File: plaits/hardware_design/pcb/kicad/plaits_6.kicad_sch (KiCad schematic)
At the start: 22 parts

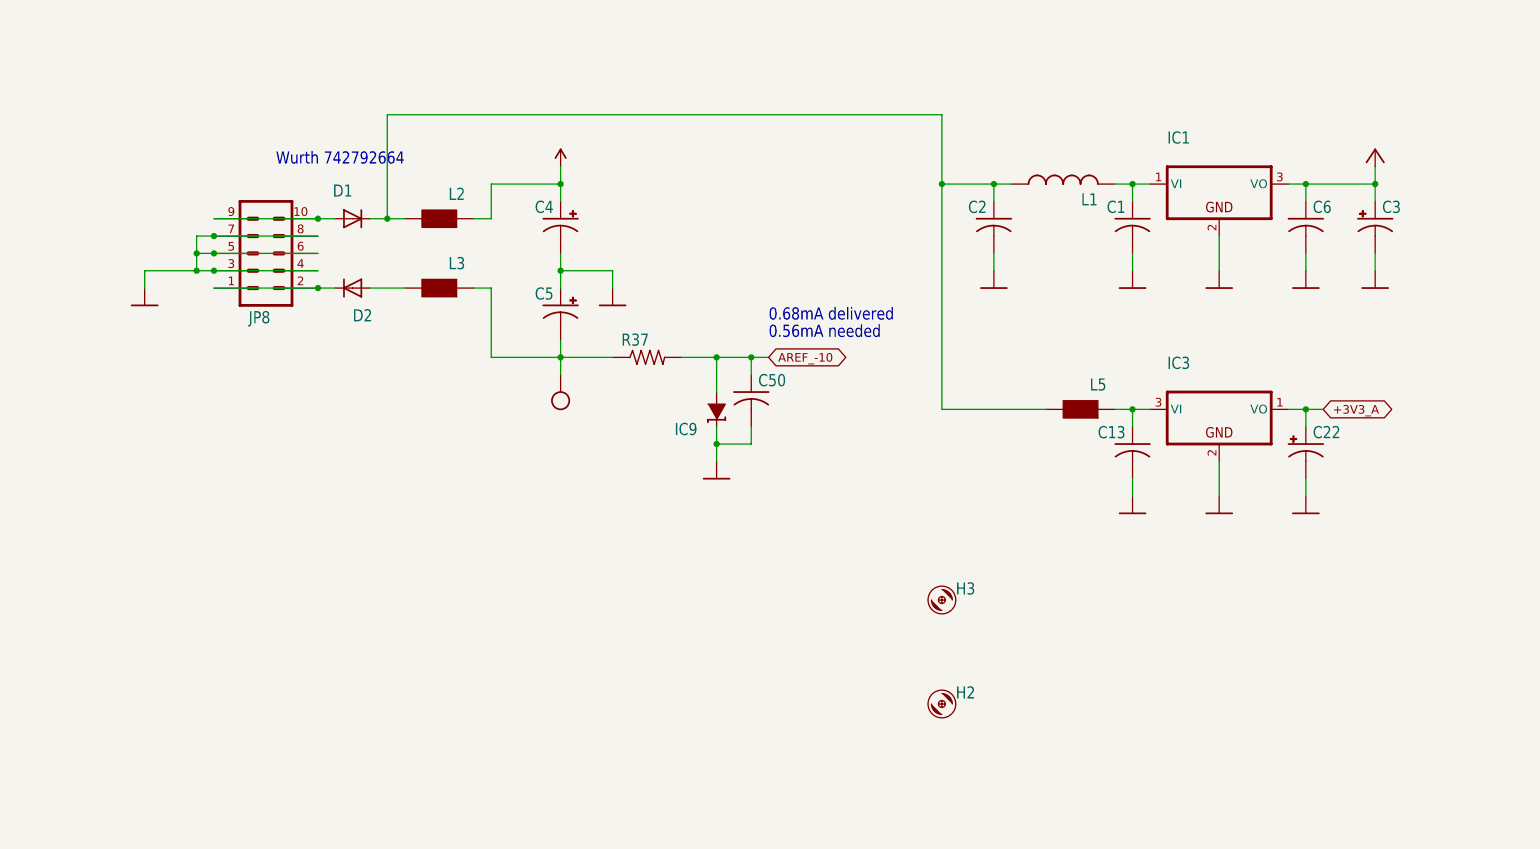
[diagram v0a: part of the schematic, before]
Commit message: plaits resized panasonic A -> B caps
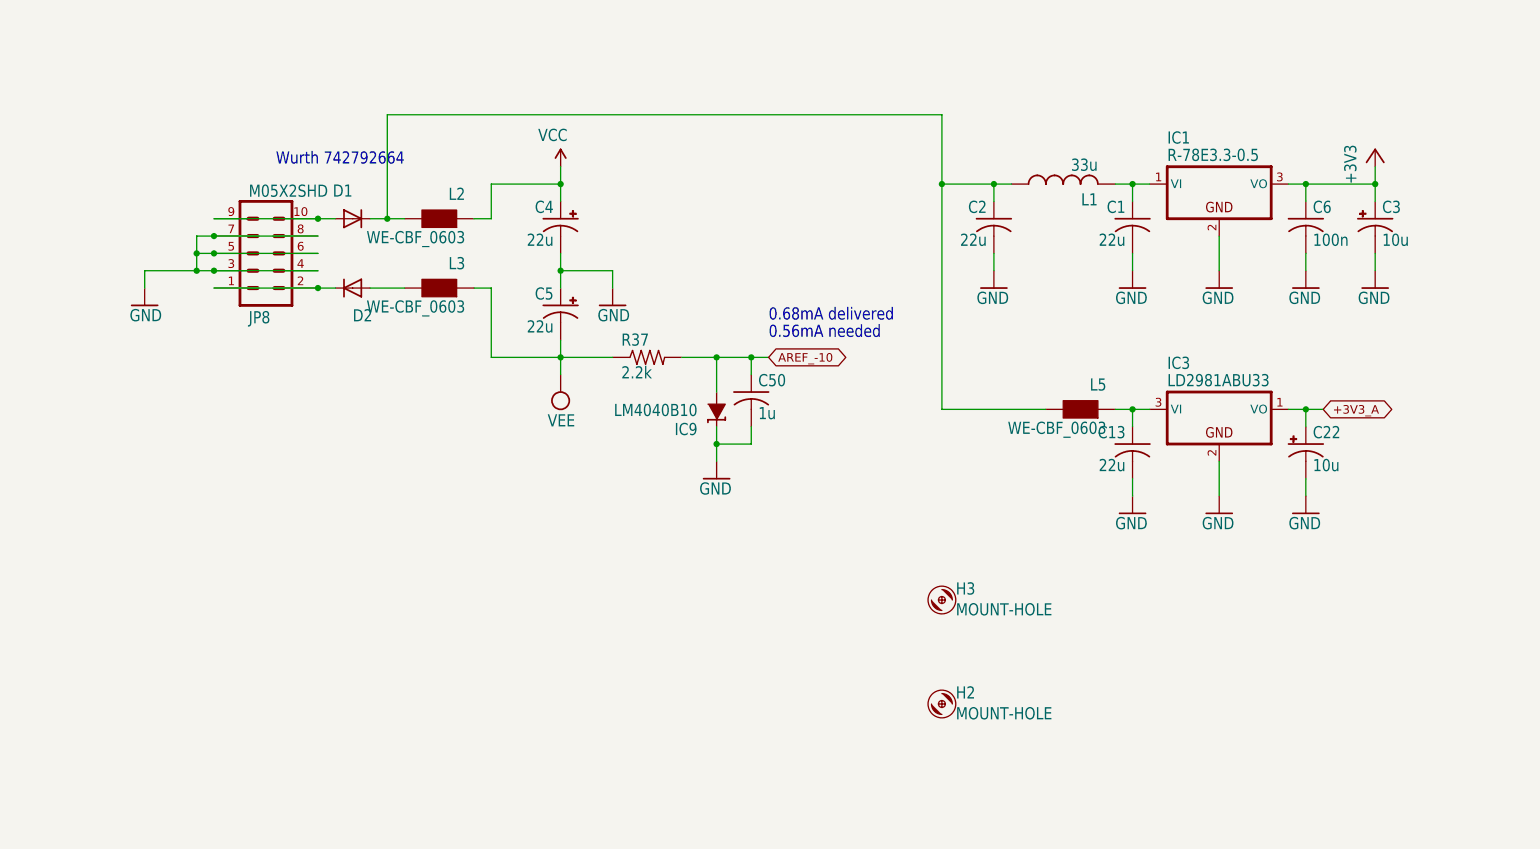
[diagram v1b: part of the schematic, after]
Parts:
- C1, C13, C2: value (none) -> 22u; footprint (none) -> plaits:C1206
- C22, C3: value (none) -> 10u; footprint (none) -> plaits:PANASONIC_B
- C4, C5: value (none) -> 22u; footprint (none) -> plaits:PANASONIC_B
- C50: value (none) -> 1u; footprint (none) -> plaits:C0402
- C6: value (none) -> 100n; footprint (none) -> plaits:C0402
- D1, D2: value (none) -> 1N5819HW; footprint (none) -> plaits:SOD123
- H2, H3: value (none) -> MOUNT-HOLE; footprint (none) -> plaits:3,0TINY
- IC1: value (none) -> R-78E3.3-0.5; footprint (none) -> plaits:WE78
- IC3: value (none) -> LD2981ABU33; footprint (none) -> plaits:SOT89
- IC9: value (none) -> LM4040B10; footprint (none) -> plaits:DBZ_R-PDSO-G3
- JP8: value (none) -> M05X2SHD; footprint (none) -> plaits:2X5-SHROUDED
- L1: value (none) -> 33u; footprint (none) -> plaits:L2012C
- L2, L3, L5: value (none) -> WE-CBF_0603; footprint (none) -> plaits:0603
- R37: value (none) -> 2.2k; footprint (none) -> plaits:R0402
